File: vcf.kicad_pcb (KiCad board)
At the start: 2 copper layers, 63 x 42 mm, 42 parts, among them J1 P3, J2 P5, J3 OUT, J4 IN, J5 P2, J6 P4, J7 POWER, U1 LM13700, U2 LM13700

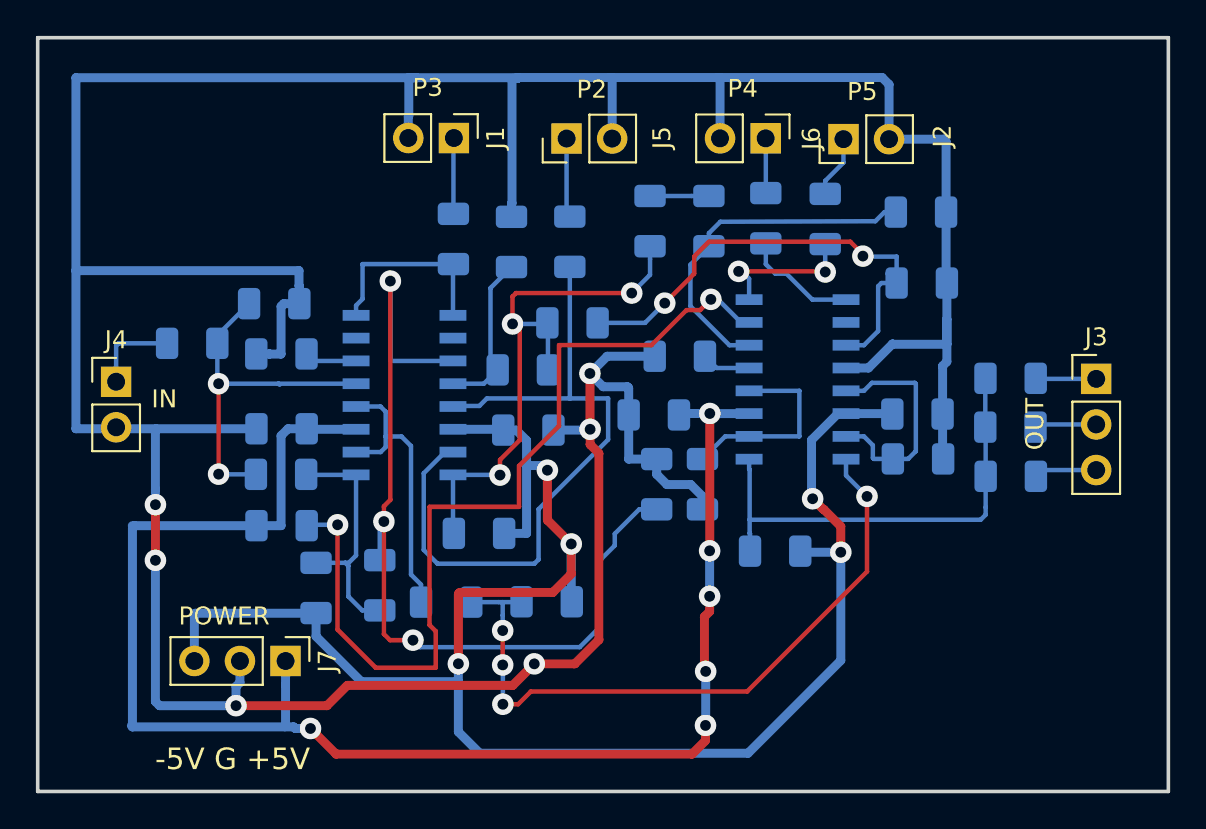
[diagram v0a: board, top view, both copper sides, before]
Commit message: Изменена плата под компоненты 0603
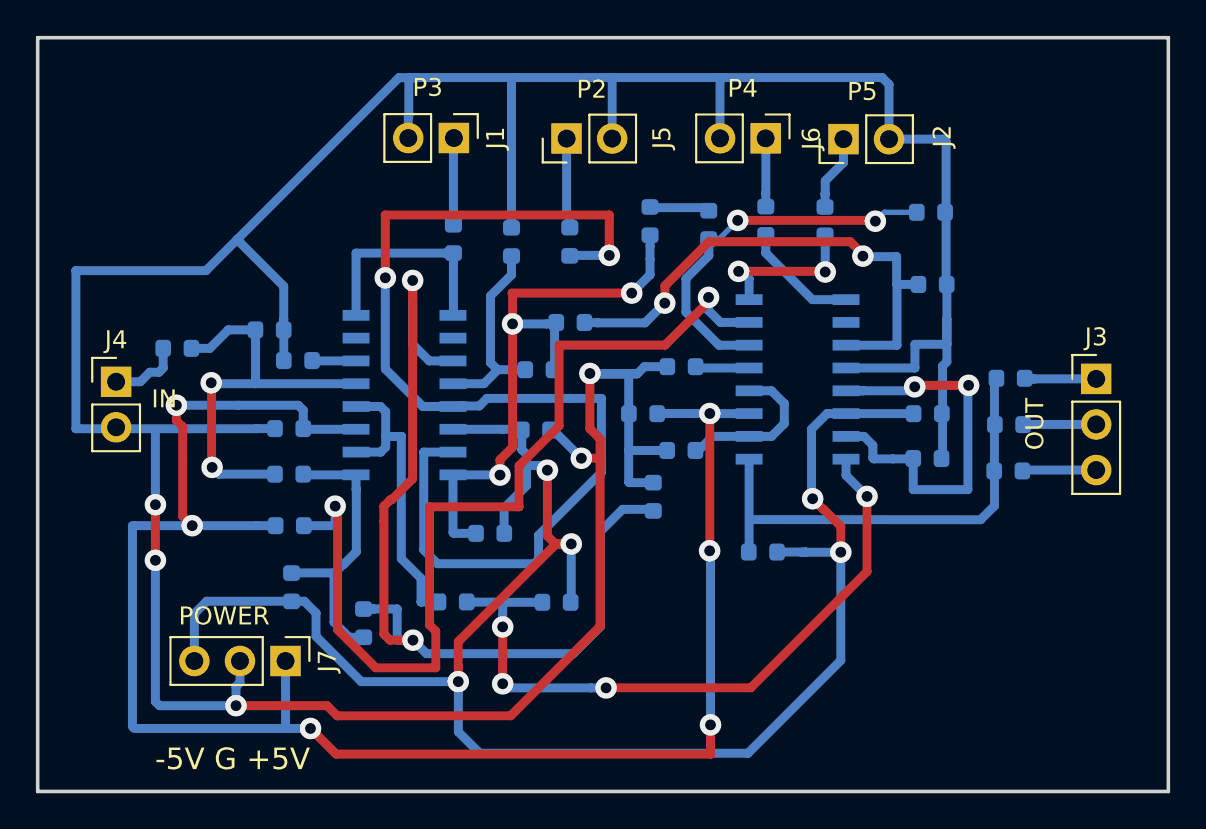
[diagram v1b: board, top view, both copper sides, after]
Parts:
- C1, C2, C3, C4, C5, C6, C7: footprint footprint:C_1206 -> footprint:c0603
- R1, R10, R11, R12, R13, R14, R15, R16, R17, R18, R19, R2, R20, R21, R22, R23, R24, R25, R26, R3, R4, R5, R6, R7, R8, R9: footprint footprint:R_1206 -> footprint:r0603
- moved R8 2.30 mm to (38.2, 52.6)
- moved R20 2.22 mm to (55.9, 43.0), turned to 180 degrees
- moved R13 1.48 mm to (32.9, 36.3)
- moved R14 1.36 mm to (34.1, 50.6)
- moved R6 0.99 mm to (34.5, 38.0)
- moved R3 0.92 mm to (48.0, 38.5)
- moved R10 0.88 mm to (27.8, 37.3)
- moved R16 0.73 mm to (54.3, 45.6)
- moved R21 0.68 mm to (60.4, 48.7)
- moved R17 0.62 mm to (45.2, 47.6)
- moved R24 0.61 mm to (69.9, 33.8)
- moved C5 0.60 mm to (53.7, 41.0)
- moved R19 0.59 mm to (55.9, 38.3)
- moved C7 0.57 mm to (69.6, 41.0)
- moved R18 0.56 mm to (69.8, 29.7)
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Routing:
- net Net-(C3-Pad1): track 39.9 -> 62.9 mm, vias 0 -> 2
- net GND: track 222.8 -> 208.0 mm, vias 6 -> 5
- net Net-(R26-Pad1): track 12.9 -> 23.6 mm, vias 0 -> 2
- net +5V: track 87.8 -> 97.8 mm
- net Net-(R10-Pad1): track 20.1 -> 23.9 mm
- net Net-(R4-Pad2): track 50.1 -> 53.2 mm
- net Net-(R16-Pad1): track 51.2 -> 54.0 mm, vias 3 -> 2
- net Net-(R20-Pad1): track 11.3 -> 9.00 mm
- net Net-(R14-Pad1): track 13.7 -> 15.9 mm
- net Net-(C1-Pad2): track 30.8 -> 33.0 mm
- net Net-(R15-Pad1): track 9.19 -> 11.3 mm
- net Net-(R22-Pad2): track 27.4 -> 29.1 mm
- net Net-(R1-Pad1): track 10.9 -> 12.4 mm
- net Net-(R11-Pad1): track 19.6 -> 20.7 mm, vias 0 -> 2
- net Net-(J3-Pad1): track 3.38 -> 4.39 mm
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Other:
- net class Default: trace_width 0.25 -> 0.5
- rule solder_mask_min_width: 0.25 -> 0.5
